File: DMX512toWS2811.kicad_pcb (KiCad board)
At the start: 2 copper layers, 140 x 110 mm, 122 parts, among them CN1 TB112-2-2-E-1, CN2 18742, CN3 B6B-PH-K-S_LF__SN_, CN4 TB111-2-3-U-1-1, CN5 TB112-2-2-E-1, CN6 TB112-2-2-E-1, IC1 MAX485ESA+, IC2 MAX485ESA+, IC3 TLP2361_TPL,E, IC4 TCK106AF,LF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

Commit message: * アートワーク作業中
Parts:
- removed NT2, NTe: NetTie_2, NetTie:NetTie-2_SMD_Pad2.0mm
- removed the TP1 at (160.8, 71.5)
- removed the TP2 at (159.2, 69.5)
- added C20: 0.1u, Capacitor_SMD:C_0603_1608Metric_Pad1.08x0.95mm_HandSolder, F.Cu at (175.9, 78.3)
- added C21: 1000p, Capacitor_SMD:C_0603_1608Metric_Pad1.08x0.95mm_HandSolder, F.Cu at (184.2, 78.1)
- added IC8: NJU77551F-TE1, SamacSys_Parts:SOT95P280X130-5N, F.Cu at (179.1, 78.7)
- added R41: 2k, Resistor_SMD:R_0603_1608Metric_Pad0.98x0.95mm_HandSolder, F.Cu at (179.7, 74.7)
- added R42: 2k, Resistor_SMD:R_0603_1608Metric_Pad0.98x0.95mm_HandSolder, F.Cu at (182.2, 78.1)
- added R43: 0, Resistor_SMD:R_0603_1608Metric_Pad0.98x0.95mm_HandSolder, F.Cu at (179.7, 71.1)
- added R44: 0, Resistor_SMD:R_0603_1608Metric_Pad0.98x0.95mm_HandSolder, F.Cu at (179.1, 81.9)
- added R45: 10k, Resistor_SMD:R_0603_1608Metric_Pad0.98x0.95mm_HandSolder, F.Cu at (176.3, 85.1)
- added R46: 10k, Resistor_SMD:R_0603_1608Metric_Pad0.98x0.95mm_HandSolder, F.Cu at (180.6, 83.8)
- moved VA1 2.50 mm to (131.8, 138.0)
- moved CA1 1.27 mm to (114.2, 114.6)
- moved D8 0.40 mm to (146.0, 111.0)
- renumbered TP3 to TP1, TP4 to TP2, TP5 to TP3
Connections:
- CN4 pad 1: GND2 -> GND
- CN6 pad 1: GND1 -> GND
- IC5 pad 22: Net-(IC5-RB1) -> OSIG_P
- IC5 pad 23: Net-(IC5-RB2) -> OSIG_N
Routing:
- net +5V: track 328.7 -> 0.00 mm
- net UART_RX: track 181.5 -> 0.00 mm, vias 8 -> 0
- net GND: track 200.4 -> 25.0 mm, vias 208 -> 16
- net VDC: track 149.4 -> 14.4 mm
- net PSMODE_SW: track 87.2 -> 0.00 mm, vias 4 -> 0
- net 485_DE: track 82.5 -> 0.00 mm, vias 2 -> 0
- net 485_nRE: track 79.8 -> 0.00 mm, vias 2 -> 0
- net Net-(IC4-VOUT): track 73.6 -> 0.00 mm
- net /5V_OUT: track 70.8 -> 0.00 mm
- net RST_SW: track 70.3 -> 0.00 mm, vias 5 -> 0
- net PWM_B: track 65.2 -> 0.00 mm, vias 2 -> 0
- net GND2: track 64.5 -> 0.00 mm
- net PWM_G: track 63.8 -> 0.00 mm, vias 2 -> 0
- net PWM_R: track 62.5 -> 0.00 mm, vias 2 -> 0
- net GND1: track 62.1 -> 0.00 mm
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- added copper zone on F.Cu, net Net-(D8-A)
- added copper zone on F.Cu, net VDC
- added copper zone on F.Cu, net VPP
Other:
- outline, holes or cut-outs redrawn

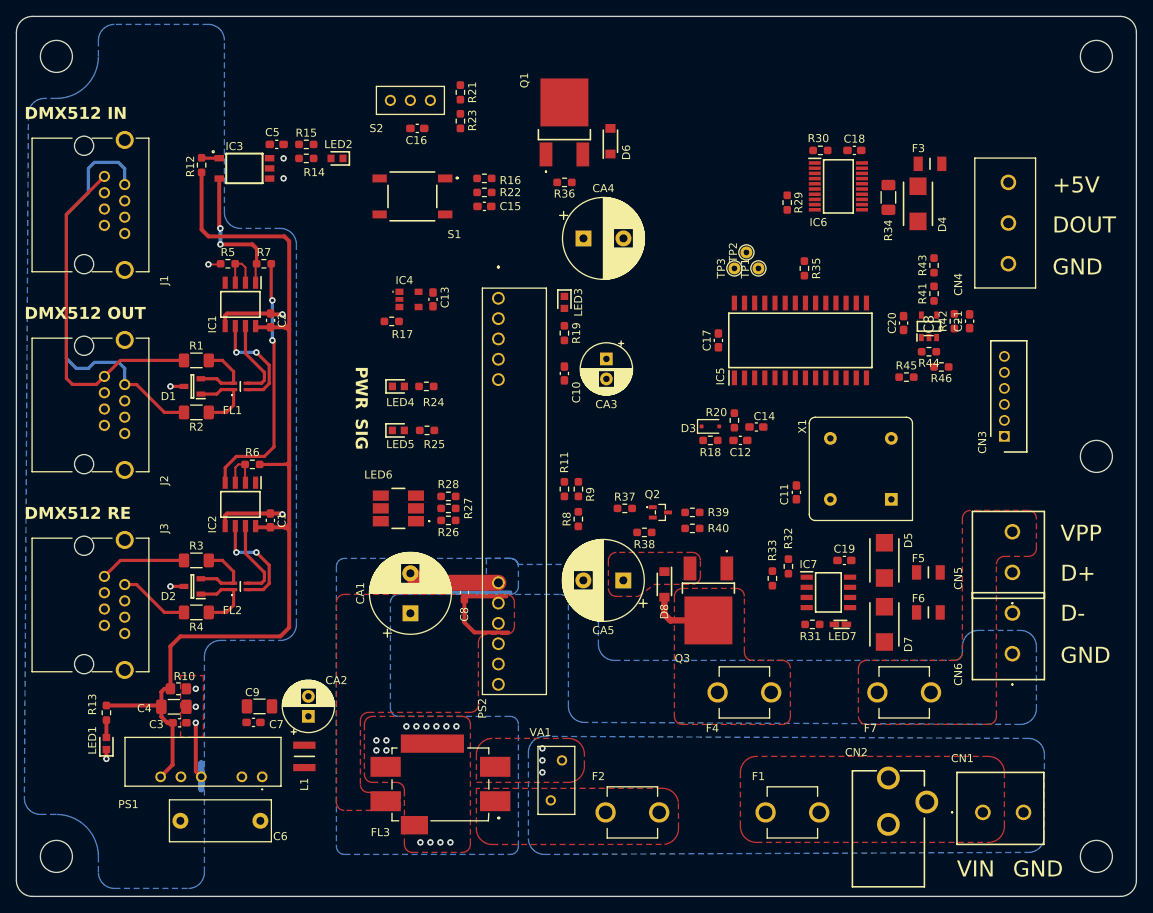
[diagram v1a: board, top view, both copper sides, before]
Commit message: * GNDパターン引き直し
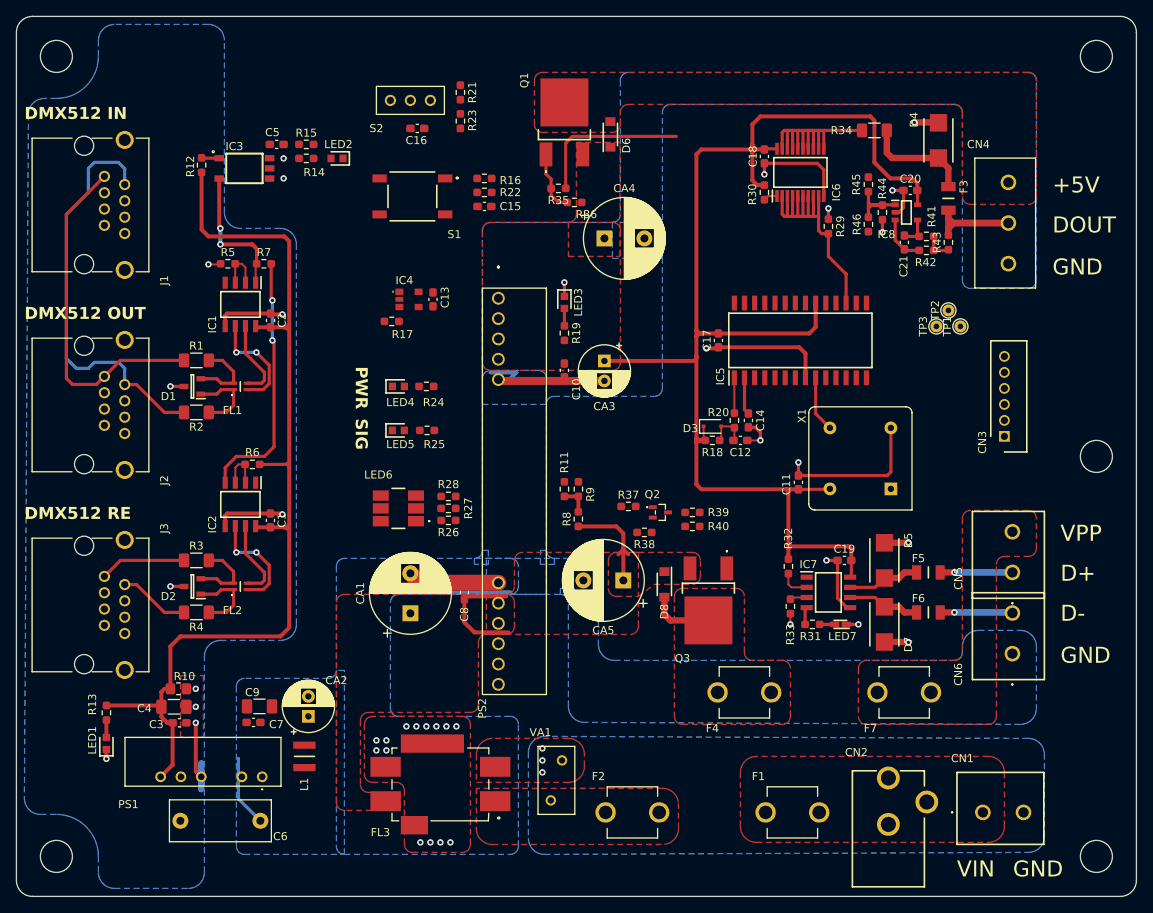
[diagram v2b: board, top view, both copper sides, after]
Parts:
- moved R35 32.3 mm to (132.8, 61.5), turned to 180 degrees
- moved TP1 26.3 mm to (183.0, 78.8)
- moved TP2 26.3 mm to (181.5, 76.8)
- moved TP3 26.3 mm to (180.0, 78.8)
- moved R45 24.6 mm to (171.5, 61.0), turned to -90 degrees
- moved R46 20.0 mm to (171.5, 66.0), turned to 90 degrees
- moved R44 18.4 mm to (173.2, 64.5), turned to 90 degrees
- moved C20 16.6 mm to (176.8, 61.8), turned to 0 degrees
- moved IC8 14.5 mm to (176.2, 64.5), turned to 0 degrees
- moved C21 12.8 mm to (176.0, 68.2), turned to -90 degrees
- moved C18 11.3 mm to (158.5, 57.5), turned to 90 degrees
- moved R42 9.52 mm to (178.8, 69.2), turned to 0 degrees
- moved R30 8.75 mm to (158.5, 62.0), turned to -90 degrees
- moved R34 8.56 mm to (172.2, 54.2), turned to 0 degrees
- moved D4 8.33 mm to (180.2, 55.5), turned to -90 degrees
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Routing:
- net +5V: track 0.00 -> 165.8 mm
- net GND: track 25.0 -> 134.2 mm, vias 16 -> 30
- net SIGOUT: track 0.00 -> 37.7 mm
- net Net-(IC6-Y1): track 0.00 -> 30.8 mm
- net 5VOUT_EN: track 0.00 -> 19.8 mm
- net /SIG_OUT: track 0.00 -> 18.6 mm
- net VDC: track 14.4 -> 28.1 mm
- net Net-(D4-Pad2): track 0.00 -> 13.6 mm
- net Net-(IC7-B): track 0.00 -> 9.09 mm
- net Net-(IC7-A): track 0.00 -> 9.09 mm
- net /D+_OUT: track 0.00 -> 9.06 mm, vias 0 -> 1
- net /D-_OUT: track 0.00 -> 9.03 mm, vias 0 -> 1
- net Net-(IC8-+INPUT): track 0.00 -> 8.65 mm
- net BAT_VOL: track 0.00 -> 8.34 mm
- net Net-(Q1-G): track 0.00 -> 7.73 mm
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- added copper zone on F.Cu, net +5V
- added copper zone on F.Cu, net /5V_OUT
